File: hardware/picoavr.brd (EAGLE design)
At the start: 36.2 x 17.8 mm, 25 parts, among them IC1 MCP1703CB, Q2 12mhz, SW1 SPST_TACT-KMR2, U3 ATMEGA328P, X1 Micro USB

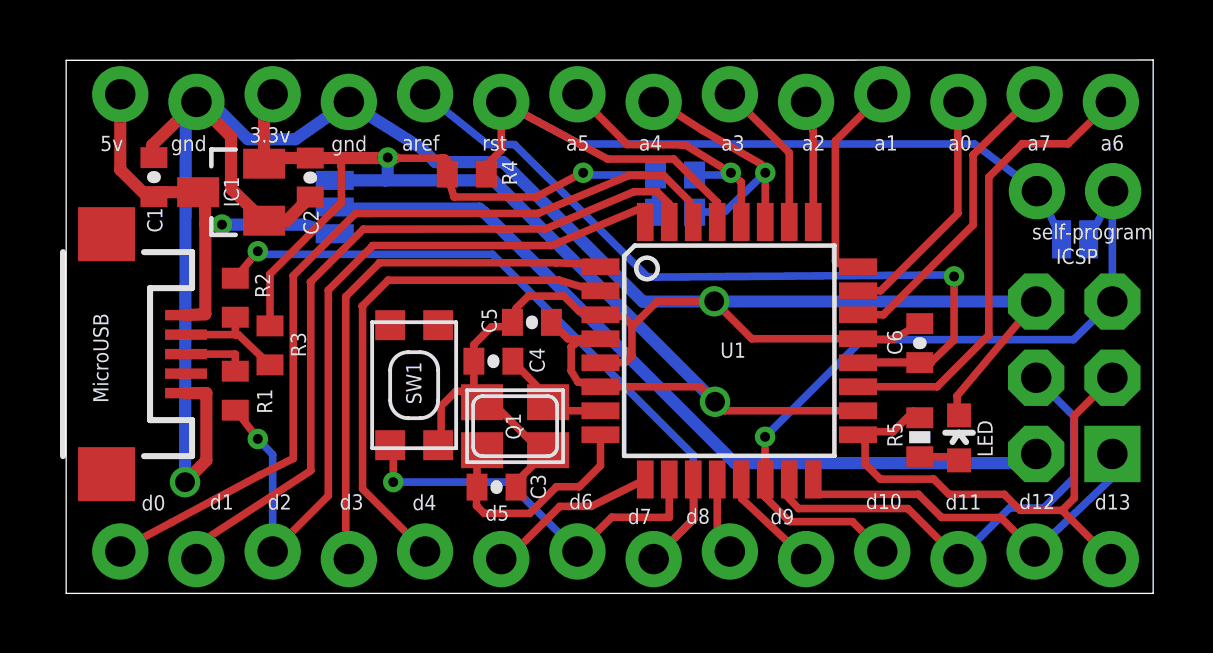
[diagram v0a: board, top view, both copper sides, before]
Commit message: add optional reset button
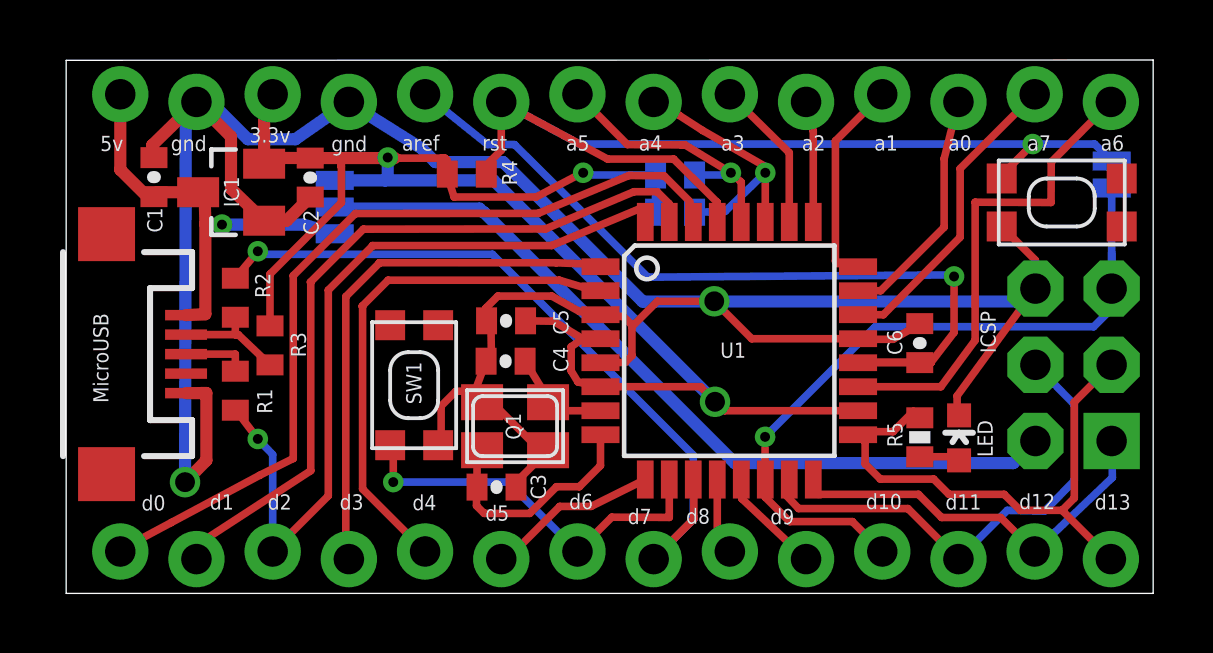
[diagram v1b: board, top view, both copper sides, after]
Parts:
- removed SELF_PROGRAM: (no value), SparkFun-Passives:1X02
- added SW2: SPST_TACT-KMR2, adafruit:KMR2
- SJ1: value (none) -> SJ1
- moved SJ2 2.48 mm to (34.9, 14.0), turned to 270 degrees
- moved C5 0.87 mm to (14.7, 9.09)
- moved JSP 0.43 mm to (33.6, 7.62)
- moved C3 0.41 mm to (14.7, 7.74)
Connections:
- net GND: now also SW2.1
- net ISP_RESET: no longer SELF_PROGRAM.2
- net RESET: now also SW2.2; no longer SELF_PROGRAM.1
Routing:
- net GND: track 93.6 -> 97.0 mm
- net RESET: track 32.3 -> 34.2 mm, vias 0 -> 1
- net A0: track 9.16 -> 7.98 mm
- net VCC: track 56.5 -> 57.3 mm
- net A6: track 15.4 -> 16.0 mm
- net MOSI: track 16.0 -> 16.5 mm
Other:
- board text removed: "self-program"

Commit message: move reset for silk screen
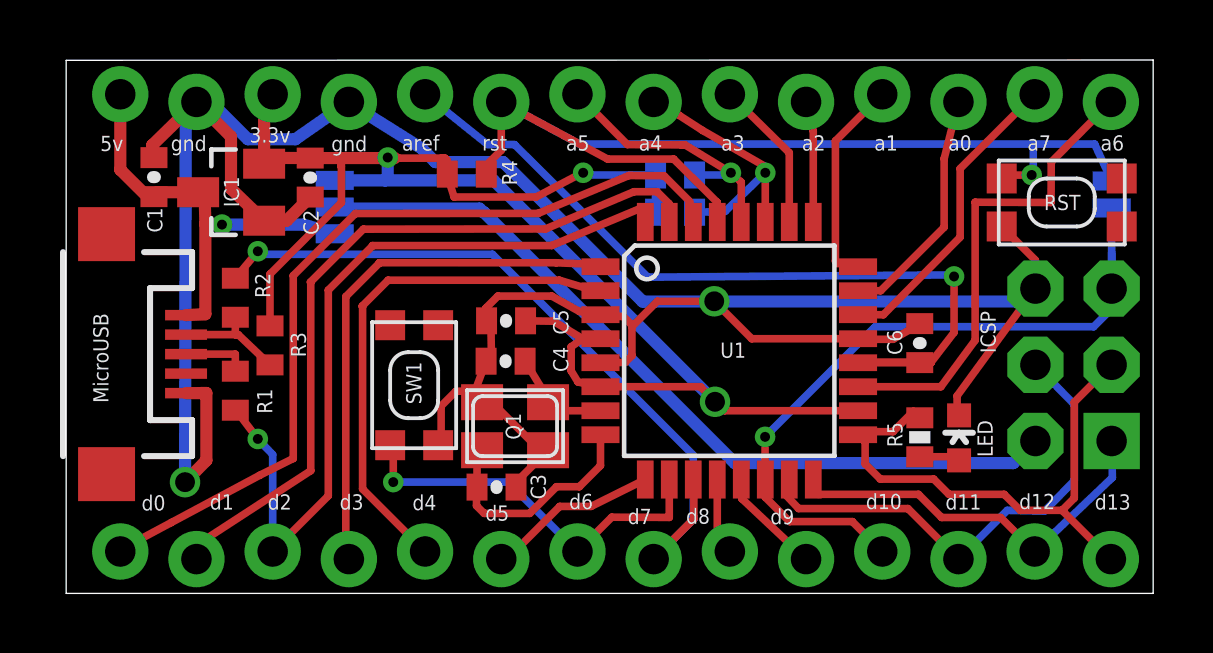
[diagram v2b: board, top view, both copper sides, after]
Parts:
- moved SJ2 0.66 mm to (34.9, 13.3)
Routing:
- net RESET: track 34.2 -> 35.4 mm
- net ISP_RESET: track 25.2 -> 24.6 mm
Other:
- board text added: "RST"
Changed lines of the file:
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@@
 <setting verticaltext="up"/>
 </settings>
-<grid distance="0.05" unitdist="inch" unit="inch" style="lines" multiple="1" display="yes" altdistance="0.001" altunitdist="inch" altunit="inch"/>
+<grid distance="0.05" unitdist="inch" unit="inch" style="lines" multiple="1" display="yes" altdistance="0.0001" altunitdist="inch" altunit="inch"/>
 <layers>
 <layer number="1" name="Top" color="4" fill="1" visible="yes" active="yes"/>
@@
 <text x="11.6992375" y="13.416278125" size="0.508" layer="122" font="vector" ratio="12" rot="MR0">3.3v</text>
 <text x="11.7195625" y="11.5824" size="0.508" layer="122" font="vector" ratio="12" rot="MR0">5.0v</text>
-<text x="33.461959375" y="13.7820375" size="0.508" layer="122" font="vector" ratio="12" rot="MR0">self-Program</text>
+<text x="33.766759375" y="13.0962375" size="0.508" layer="122" font="vector" ratio="12" rot="MR0">self-Program</text>
 <polygon width="0.254" layer="122">
 <vertex x="25.63146875" y="4.46033125" curve="-9.500029"/>
@@
 <text x="11.625759375" y="7.012359375" size="0.508" layer="121" font="vector" ratio="12" rot="R90" align="center">SW1</text>
 <text x="14.943" y="5.569640625" size="0.508" layer="121" font="vector" ratio="12" rot="R90" align="center">Q1</text>
+<text x="33.241159375" y="13.032159375" size="0.508" layer="121" font="vector" ratio="12" rot="R180" align="center">RST</text>
 </plain>
 <attributes>
@@
 <attribute name="VALUE" x="8.9916" y="12.7777" size="0.02" layer="28" rot="MR90"/>
 </element>
-<element name="SJ2" library="SparkFun-Passives" package="SJ_2S-NO" value="SOLDERJUMPERNO" x="34.888259375" y="13.959640625" smashed="yes" rot="MR270"/>
+<element name="SJ2" library="SparkFun-Passives" package="SJ_2S-NO" value="SOLDERJUMPERNO" x="34.888259375" y="13.299240625" smashed="yes" rot="MR270"/>
 <element name="SW1" library="adafruit" package="KMR2" value="SPST_TACT-KMR2" x="11.6384" y="6.9397" rot="R270"/>
 <element name="SW2" library="adafruit" package="KMR2" value="SPST_TACT-KMR2" x="33.2232" y="13.0302" rot="R180"/>
@@
 <wire x1="21.7415" y1="13.0356" x2="20.2895" y2="14.4776" width="0.254" layer="1"/>
 <wire x1="14.043415625" y1="13.97458125" x2="13.870940625" y2="14.1013375" width="0.254" layer="1"/>
-<wire x1="17.1529" y1="14.978" x2="32.258" y2="14.978" width="0.254" layer="16"/>
-<wire x1="32.258" y1="14.978" x2="34.3199" y2="14.978" width="0.254" layer="16"/>
+<wire x1="17.1529" y1="14.978" x2="32.273240625" y2="14.978" width="0.254" layer="16"/>
+<wire x1="32.273240625" y1="14.978" x2="34.3199" y2="14.978" width="0.254" layer="16"/>
 <wire x1="20.2895" y1="14.4776" x2="18.088503125" y2="14.4776" width="0.254" layer="1"/>
 <wire x1="18.088503125" y1="14.4776" x2="14.5415" y2="16.383" width="0.254" layer="1"/>
 <wire x1="13.870940625" y1="14.1013375" x2="14.5415" y2="14.771896875" width="0.254" layer="1"/>
 <wire x1="14.5415" y1="14.771896875" x2="14.5415" y2="16.383" width="0.254" layer="1"/>
-<wire x1="34.3199" y1="14.978" x2="34.888259375" y2="14.409640625" width="0.254" layer="16"/>
+<wire x1="34.3199" y1="14.978" x2="34.888259375" y2="13.749240625" width="0.254" layer="16"/>
 <contactref element="SW2" pad="2"/>
 <wire x1="31.2232" y1="13.8302" x2="31.2232" y2="13.9432" width="0.254" layer="1"/>
-<wire x1="31.2232" y1="13.9432" x2="32.258" y2="14.978" width="0.254" layer="1"/>
-<via x="32.258" y="14.978" extent="1-16" drill="0.3302"/>
+<wire x1="31.2232" y1="13.9432" x2="32.1945" y2="13.9432" width="0.254" layer="1"/>
+<wire x1="32.1945" y1="13.9432" x2="32.222440625" y2="13.947140625" width="0.254" layer="1"/>
+<via x="32.222440625" y="13.947140625" extent="1-16" drill="0.3302"/>
+<wire x1="32.222440625" y1="13.947140625" x2="32.27578125" y2="13.947140625" width="0.254" layer="16"/>
+<wire x1="32.27578125" y1="13.947140625" x2="32.273240625" y2="14.978" width="0.254" layer="16"/>
 </signal>
 <signal name="USB_DPLUS">
@@
 <wire x1="26.2455" y1="2.393" x2="27.2415" y2="1.397" width="0.254" layer="1"/>
 <wire x1="34.8869" y1="10.16" x2="34.8869" y2="11.8092" width="0.254" layer="16"/>
-<wire x1="34.8869" y1="11.8092" x2="34.888259375" y2="13.509640625" width="0.254" layer="16"/>
+<wire x1="34.8869" y1="11.8092" x2="34.888259375" y2="12.849240625" width="0.254" layer="16"/>
 <wire x1="34.8869" y1="11.3665" x2="34.8869" y2="10.16" width="0.254" layer="16"/>
 <wire x1="23.3353" y1="5.2188" x2="27.0065" y2="8.89" width="0.254" layer="16"/>
